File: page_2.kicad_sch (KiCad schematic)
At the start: 75 parts, among them J2 Micro_SD_Card_Det_Hirose_DM3AT, J201 Conn_01x05, J601 USB_C_Receptacle_USB2.0_16P, SW201 BOOT, SW202 RESET, T201 TP 201, U203 TPS3840DL42DBVR, U3 TCA9535PWR, U401 W25N01GVZEIG, U601 USBLC6-2SC6, U602 USBLC6-2SC6, U702 ATECC608B-SSHDA, U801 ASM330LHHTR, U802 TMP1075DGKR, U901 TPS22918TDBVTQ1, U902 SN74AXC4T245QPWRQ1, U903 SN74AXC4T245QPWRQ1

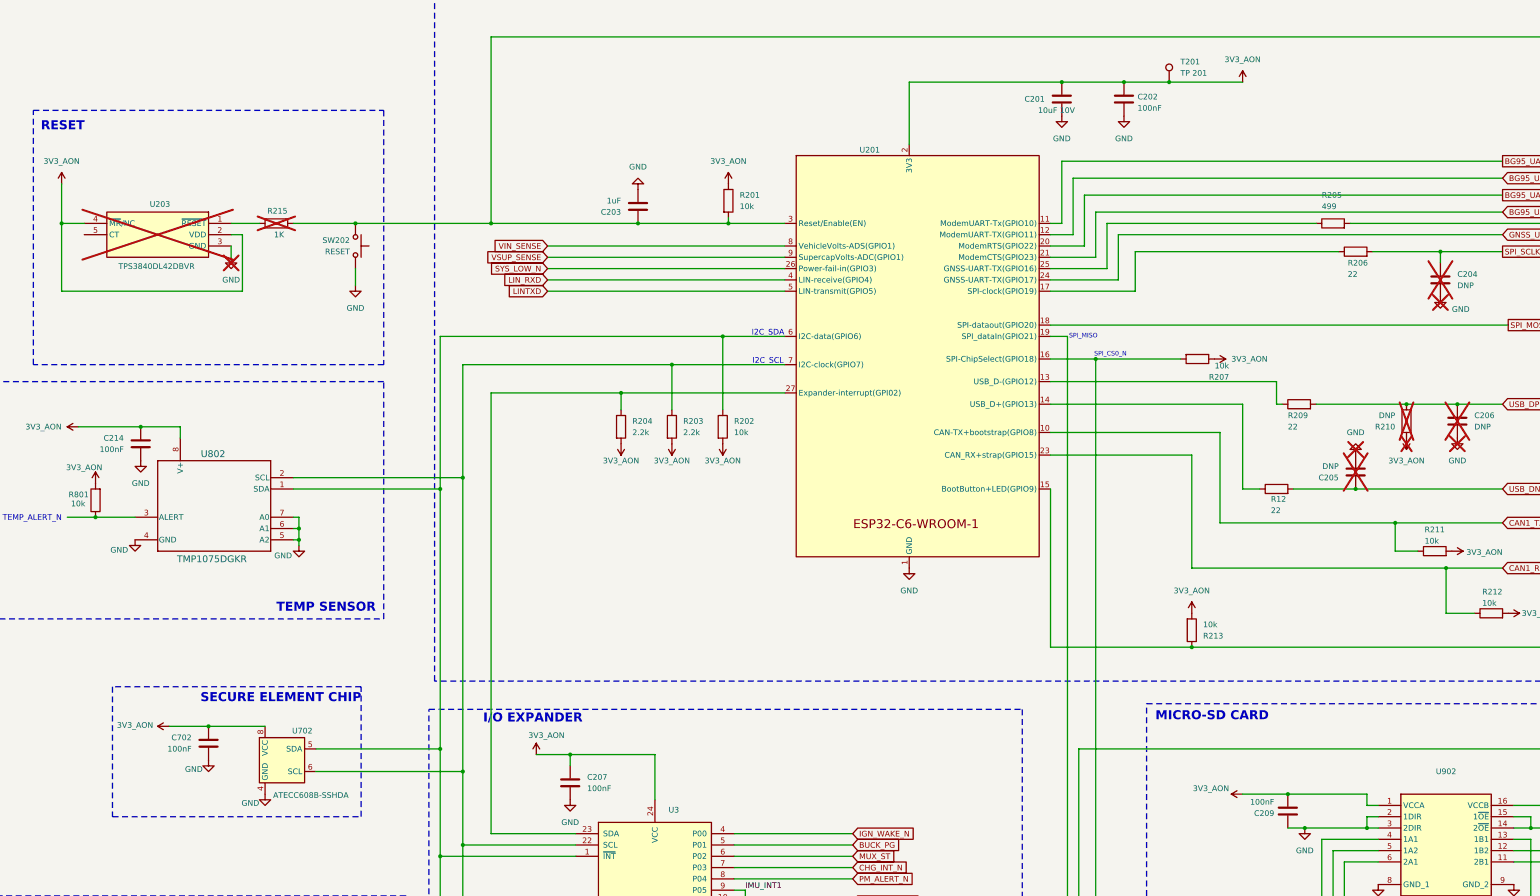
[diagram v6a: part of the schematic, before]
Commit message: Update BG95 schematic and power nets
This commit revises the tracker schematic to match the updated BG95 and power-distribution design. It adds missing power flags and net labels, updates component references and footprints, adds coaxial and connector symbols, and swaps several passives/ferrite beads to better reflect the final BOM. The netlist is also cleaned up by renaming references and correcting no-connect/power pin assignments so the KiCad project remains consistent and ERC-friendly.
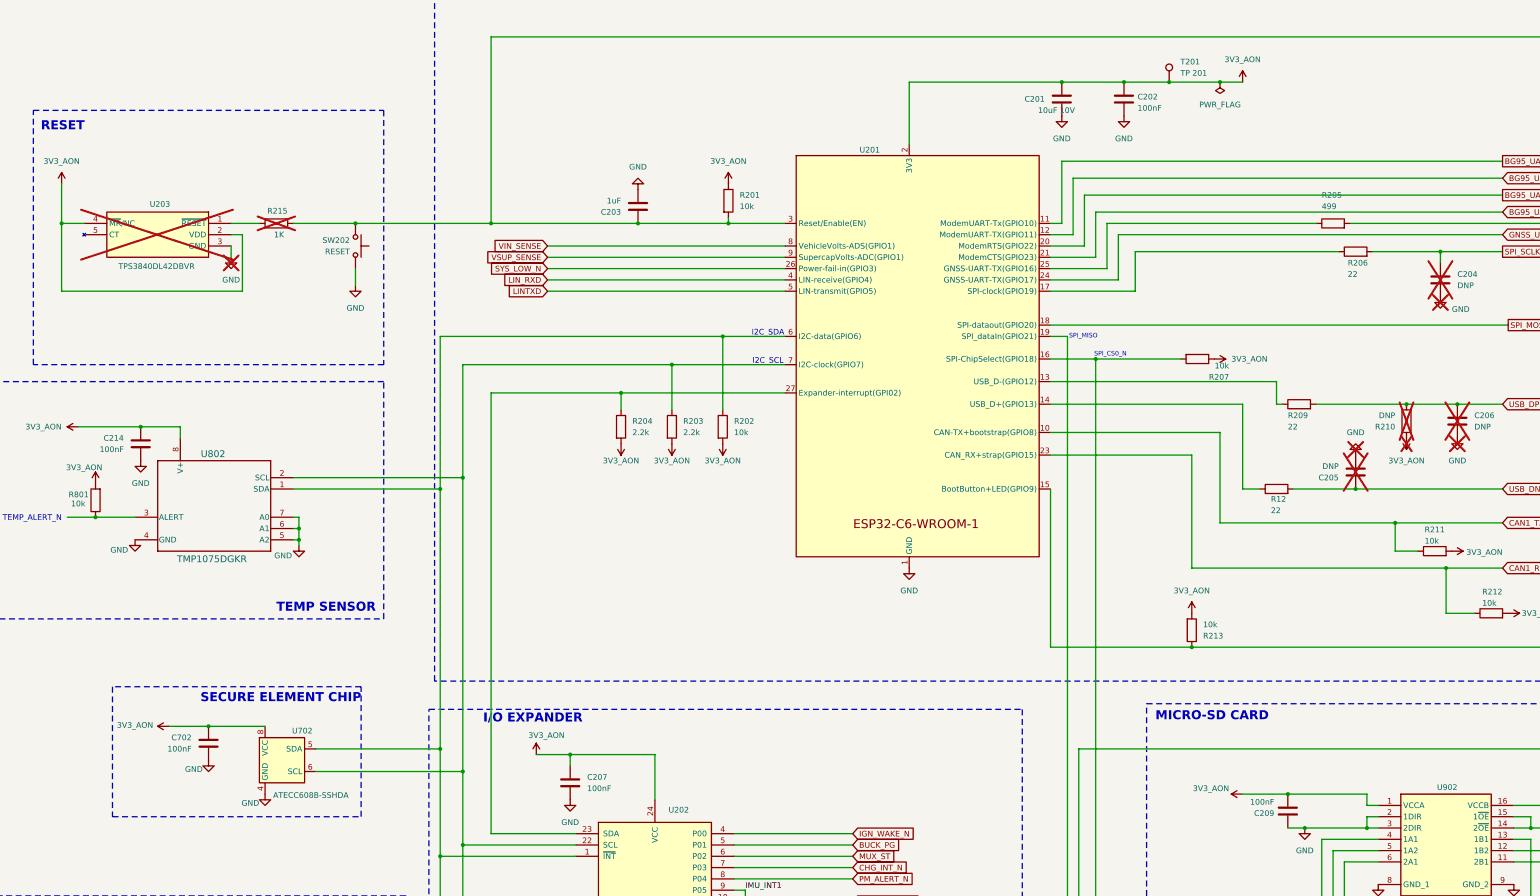
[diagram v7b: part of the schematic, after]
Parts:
- renumbered U3 to U202
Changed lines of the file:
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@@
 	)
 	(junction
+		(at 331.47 55.88)
+		(diameter 0)
+		(color 0 0 0 0)
+	)
+	(junction
 		(at 171.45 308.61)
 		(diameter 0)
@@
 	(wire
 		(pts
-			(xy 309.88 55.88) (xy 336.55 55.88)
+			(xy 309.88 55.88) (xy 331.47 55.88)
 		)
 		(stroke
@@
 	(wire
 		(pts
+			(xy 331.47 55.88) (xy 336.55 55.88)
+		)
+		(stroke
+			(width 0)
+			(type default)
+		)
+	)
+	(wire
+		(pts
 			(xy 364.49 218.44) (xy 367.03 218.44)
 		)
@@
 	)
 	(symbol
+		(lib_id "power:PWR_FLAG")
+		(at 331.47 55.88 180)
+		(unit 1)
+		(body_style 1)
+		(exclude_from_sim no)
+		(in_bom yes)
+		(on_board yes)
+		(in_pos_files yes)
+		(dnp no)
+		(fields_autoplaced yes)
+		(property "Reference" "#FLG01"
+			(at 331.47 57.785 0)
+			(hide yes)
+			(show_name no)
+			(do_not_autoplace no)
+			(effects
+				(font
+					(size 1.27 1.27)
+				)
+			)
+		)
+		(property "Value" "PWR_FLAG"
+			(at 331.47 60.96 0)
+			(show_name no)
+			(do_not_autoplace no)
+			(effects
+				(font
+					(size 1.27 1.27)
+				)
+			)
+		)
+		(property "Footprint" ""
+			(at 331.47 55.88 0)
+			(hide yes)
+			(show_name no)
+			(do_not_autoplace no)
+			(effects
+				(font
+					(size 1.27 1.27)
+				)
+			)
+		)
+		(property "Datasheet" ""
+			(at 331.47 55.88 0)
+			(hide yes)
+			(show_name no)
+			(do_not_autoplace no)
+			(effects
+				(font
+					(size 1.27 1.27)
+				)
+			)
+		)
+		(property "Description" "Special symbol for telling ERC where power comes from"
+			(at 331.47 55.88 0)
+			(hide yes)
+			(show_name no)
+			(do_not_autoplace no)
+			(effects
+				(font
+					(size 1.27 1.27)
+				)
+			)
+		)
+		(pin "1"
+		)
+		(instances
+			(project "Tracker"
+				(path "/d199d368-1586-417b-b5ba-1502c361dff2"
+					(reference "#FLG01")
+					(unit 1)
+				)
+			)
+		)
+	)
+	(symbol
 		(lib_id "power:VCC")
 		(at 71.12 78.74 0)
@@
 		(dnp no)
 		(property "Reference" "U902"
-			(at 382.27 210.82 0)
+			(at 382.524 214.376 0)
 			(show_name no)
 			(do_not_autoplace no)
@@
 		(in_pos_files yes)
 		(dnp no)
-		(property "Reference" "U3"
+		(property "Reference" "U202"
 			(at 207.518 219.456 0)
 			(show_name no)
@@
 			(project "Tracker"
 				(path "/d199d368-1586-417b-b5ba-1502c361dff2"
-					(reference "U3")
+					(reference "U202")
 					(unit 1)
 				)

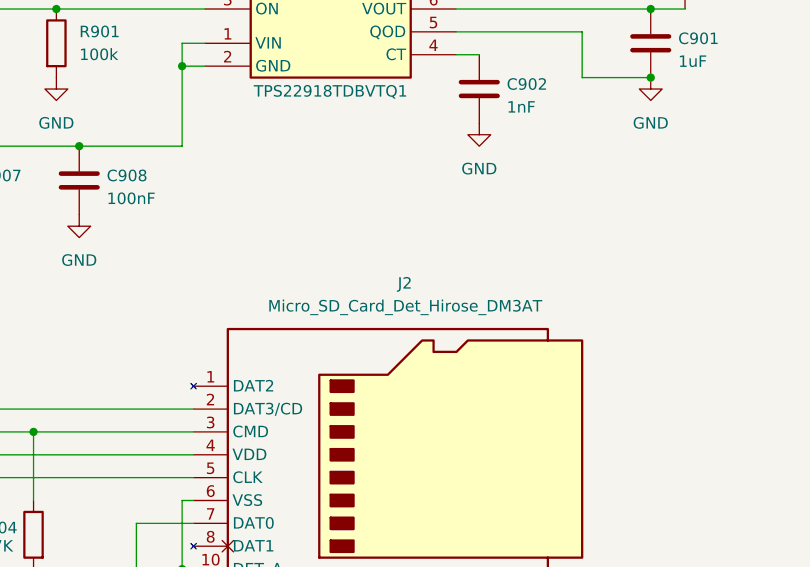
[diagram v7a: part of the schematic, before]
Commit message: Add GNSS and power protection
This update expands the Tracker schematic with vehicle input protection, GNSS receiver connectivity, and additional power/measurement components. It also refreshes KiCad symbol metadata and designator assignments, and renames the page-2 connector reference from J2 to J901 to match the updated schematic and BOM.
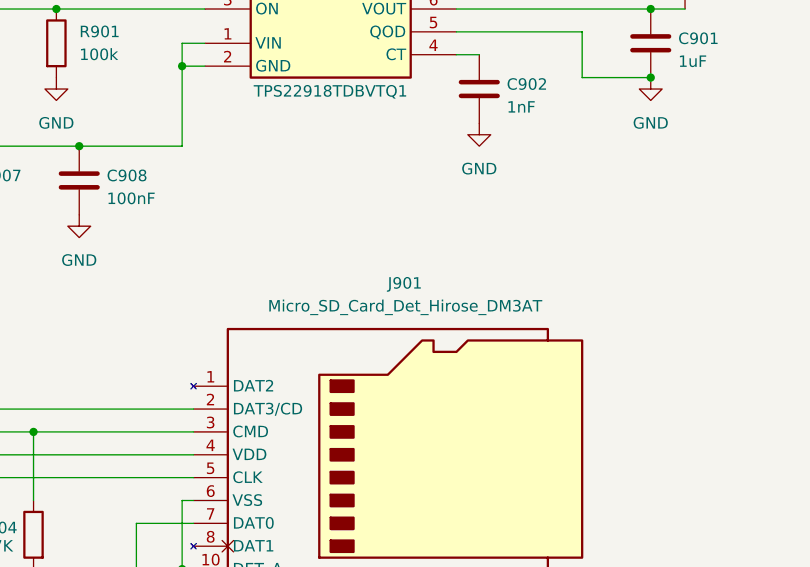
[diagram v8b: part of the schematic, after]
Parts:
- renumbered J2 to J901
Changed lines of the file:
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@@
 		(dnp no)
 		(fields_autoplaced yes)
-		(property "Reference" "J2"
+		(property "Reference" "J901"
 			(at 485.775 236.22 0)
 			(show_name no)
@@
 			(project "Tracker"
 				(path "/d199d368-1586-417b-b5ba-1502c361dff2"
-					(reference "J2")
+					(reference "J901")
 					(unit 1)
 				)
